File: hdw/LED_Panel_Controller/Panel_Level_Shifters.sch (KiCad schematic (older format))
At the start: 0 parts

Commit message: log's first
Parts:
- added C? (x2): 0.1uF, Capacitors_SMD:C_0603, symbol Custom_Library:C_Custom
- added R? (x2): 10K, Resistors_SMD:R_0603, symbol Custom_Library:R_Custom
- added RN? (x2): 10k, Resistors_SMD:R_Array_Convex_8x0602, symbol Device:R_Pack08
- added U? (x2): 74VHC541, Package_DFN_QFN:WQFN-20-1EP_2.5x4.5mm_P0.5mm_EP1x2.9mm, symbol Custom_Library:74VHC541
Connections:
- net labels added: +3.3V, +5V, GND, ~IO_Level_Shift_Enable
- wire segments 0 -> 94
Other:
- note added: "I/O Buffers"

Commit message: lots of schematic progress
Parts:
- added RN? (x2): 10k, Resistors_SMD:R_Array_Convex_8x0602, symbol Device:R_Pack08
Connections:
- net labels added: B0_POS3P3, B0_POS5, B1_POS3P3, B1_POS5, G0_POS3P3, G0_POS5, G1_POS3P3, G1_POS5, Panel_CLK_POS3P3, Panel_CLK_POS5, Panel_LAT_POS3P3, Panel_LAT_POS5, R0_POS3P3, R0_POS5, R1_POS3P3, R1_POS5, Row_A_POS3P3, Row_A_POS5, Row_B_POS3P3, Row_B_POS5, Row_C_POS3P3, Row_C_POS5, Row_D_POS3P3, Row_D_POS5, Row_E_POS3P3, Row_E_POS5, ~Panel_OE_POS3P3, ~Panel_OE_POS5
- wire segments 94 -> 172
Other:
- note removed: "I/O Buffers"
- moved on the sheet: C?, R?

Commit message: fixed level shifter sheet
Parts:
- removed R? (x2): 10K, Resistors_SMD:R_0603, symbol Custom_Library:R_Custom
- removed RN? (x4): 10k, Resistors_SMD:R_Array_Convex_8x0602, symbol Device:R_Pack08
- removed U? (x2): 74VHC541, Package_DFN_QFN:WQFN-20-1EP_2.5x4.5mm_P0.5mm_EP1x2.9mm, symbol Custom_Library:74VHC541
- added R? (x32): 10K, Resistors_SMD:R_0603, symbol Custom_Library:R_Custom
- added R? (x28): 10, Resistors_SMD:R_0402, symbol Custom_Library:R_Custom
- added U? (x2): 74HCT541, Housings_SSOP:SSOP-20_4.4x6.5mm_Pitch0.65mm, symbol 74xx:74HCT541
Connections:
- net labels added: ~Panel_Level_Shift_Enable
- net labels removed: ~IO_Level_Shift_Enable
- wire segments 172 -> 100
- no-connect marks 0 -> 2

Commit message: more schematic progress
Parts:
- removed U?: 74HCT541, Housings_SSOP:SSOP-20_4.4x6.5mm_Pitch0.65mm, symbol 74xx:74HCT541
- added U?: 74HCT541, Housings_SSOP:SSOP-20_4.4x6.5mm_Pitch0.65mm, symbol 74xx:74HCT541
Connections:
- net +5V: now also U?.20 (VCC)
- net GND: now also U?.10 (GND)
- net ~Panel_Level_Shift_Enable: now also U?.1 (G1), U?.19 (G2)
- net at R?.1, R?.1: now also U?.2 (A0)
- net at R?.1, R?.1: now also U?.3 (A1)
- net at R?.1, R?.1: now also U?.4 (A2)
- net at R?.1, R?.1: now also U?.5 (A3)
- net at R?.1, R?.1: now also U?.6 (A4)
- net at R?.1, R?.1: now also U?.7 (A5)
- net at R?.1, R?.1: now also U?.8 (A6)
- net at R?.1, R?.1: now also U?.9 (A7)
- net at R?.1, R?.1: now also U?.11 (Y7)
- net at R?.1, R?.1: now also U?.12 (Y6)
- net at R?.1, R?.1: now also U?.13 (Y5)
- net at R?.1, R?.1: now also U?.14 (Y4)
- net at R?.1, R?.1: now also U?.15 (Y3)
- net at R?.1, R?.1: now also U?.16 (Y2)
- net at R?.1, R?.1: now also U?.17 (Y1)
- net at R?.1, R?.1: now also U?.18 (Y0)
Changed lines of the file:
@@
-$EndComp
-$Comp
-L 74xx:74HCT541 U?
-U 1 1 60236D71
-P 5280 4750
-F 0 "U?" H 4980 5400 50  0000 C CNN
-F 1 "74HCT541" H 4980 4100 50  0000 C CNN
-F 2 "Housings_SSOP:SSOP-20_4.4x6.5mm_Pitch0.65mm" H 5280 4750 50  0001 C CNN
-F 3 "http://www.ti.com/lit/gpn/sn74HCT541" H 5280 4750 50  0001 C CNN
-F 4 "296-26499-1-ND" H 5280 4750 50  0001 C CNN "Digi-Key PN"
-	1    5280 4750
-	1    0    0    -1
 $EndComp
 $Comp
@@
 	0    -1   1    0
 $EndComp
+$Comp
+L 74xx:74HCT541 U?
+U 1 1 6019D5B0
+P 5280 4750
+F 0 "U?" H 4980 5400 50  0000 C CNN
+F 1 "74HCT541" H 4980 4100 50  0000 C CNN
+F 2 "Housings_SSOP:SSOP-20_4.4x6.5mm_Pitch0.65mm" H 5280 4750 50  0001 C CNN
+F 3 "http://www.ti.com/lit/gpn/sn74HCT541" H 5280 4750 50  0001 C CNN
+F 4 "296-26499-1-ND" H 5280 4750 50  0001 C CNN "Digi-Key PN"
+	1    5280 4750
+	1    0    0    -1
+$EndComp
 $EndSCHEMATC

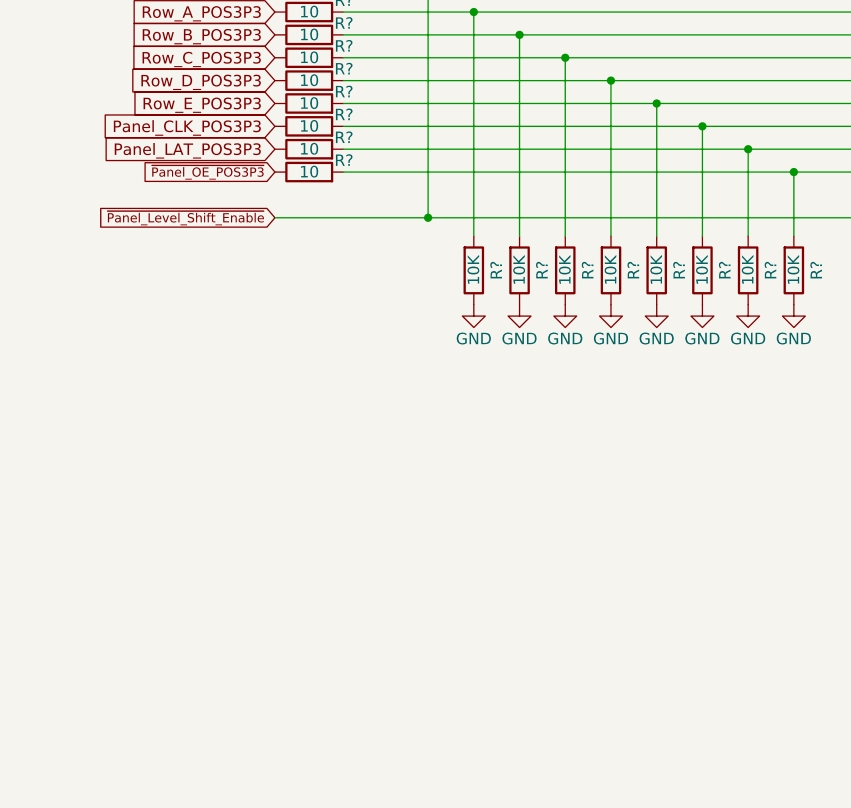
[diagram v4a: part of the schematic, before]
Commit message: Added panel dimming OR gate
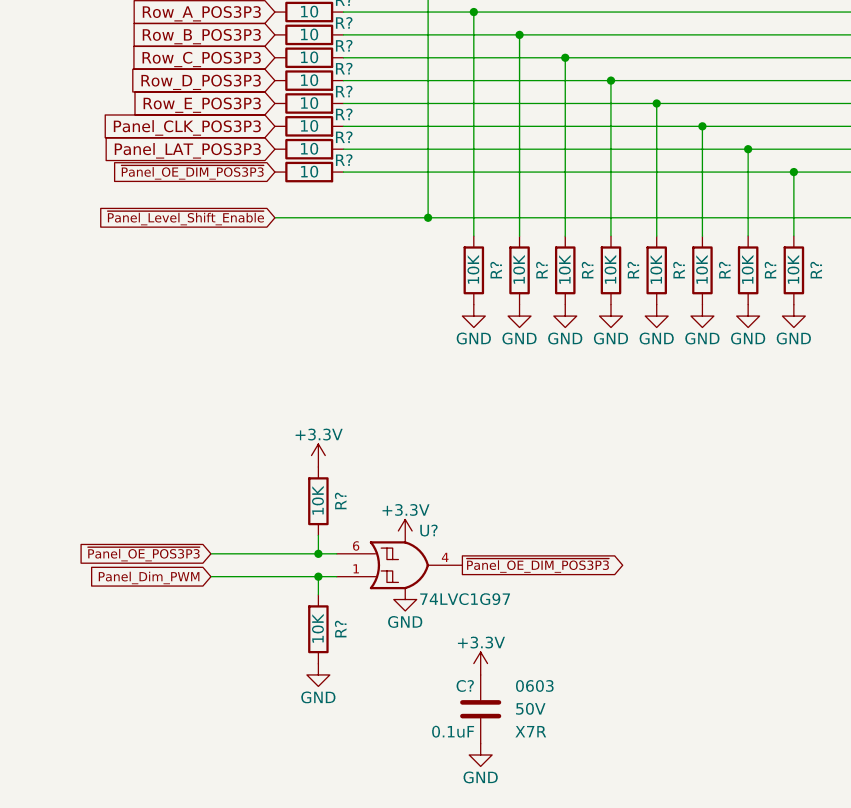
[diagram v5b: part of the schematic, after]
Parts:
- added C?: 0.1uF, Capacitors_SMD:C_0603, symbol Custom_Library:C_Custom
- added R? (x2): 10K, Resistors_SMD:R_0603, symbol Custom_Library:R_Custom
- added U?: 74LVC1G97, Package_TO_SOT_SMD:SOT-363_SC-70-6, symbol Custom_Library:74LVC1G97_Power_OR
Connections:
- net +3V3: now also C?.1, R?.1, U?.3 (VCC), U?.5 (VCC)
- net GND: now also C?.2, R?.2, U?.2 (GND)
- net ~Panel_OE_POS3P3: now also R?.2, U?.6; no longer R?.2
- new net Panel_Dim_PWM: R?.1, U?.1
- new net ~Panel_OE_DIM_POS3P3: R?.2, U?.4
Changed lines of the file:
@@
 Text GLabel 2060 4850 0    50   Input ~ 0
 Panel_LAT_POS3P3
-Text GLabel 2060 4950 0    40   Input ~ 0
-~Panel_OE_POS3P3
 Text GLabel 2060 4750 0    50   Input ~ 0
 Panel_CLK_POS3P3
@@
 	1    0    0    -1
 $EndComp
+Text GLabel 1780 6620 0    40   Input ~ 0
+~Panel_OE_POS3P3
+Text GLabel 1780 6720 0    40   Input ~ 0
+Panel_Dim_PWM
+$Comp
+L Custom_Library:74LVC1G97_Power_OR U?
+U 1 1 605B6BBC
+P 2630 6670
+F 0 "U?" H 2690 6820 50  0000 L CNN
+F 1 "74LVC1G97" H 2690 6520 50  0000 L CNN
+F 2 "Package_TO_SOT_SMD:SOT-363_SC-70-6" H 2680 6670 50  0001 C CNN
+F 3 "http://www.ti.com/lit/ds/symlink/sn74lvc1g97.pdf" H 2680 6670 50  0001 C CNN
+	1    2630 6670
+	1    0    0    -1
+$EndComp
+$Comp
+L power:GND #PWR?
+U 1 1 605B933E
+P 2630 6770
+F 0 "#PWR?" H 2630 6520 50  0001 C CNN
+F 1 "GND" H 2630 6620 50  0000 C CNN
+F 2 "" H 2630 6770 50  0001 C CNN
+F 3 "" H 2630 6770 50  0001 C CNN
+	1    2630 6770
+	1    0    0    -1
+$EndComp
+$Comp
+L power:+3.3V #PWR?
+U 1 1 605B9C84
+P 2630 6570
+F 0 "#PWR?" H 2630 6420 50  0001 C CNN
+F 1 "+3.3V" H 2630 6710 50  0000 C CNN
+F 2 "" H 2630 6570 50  0001 C CNN
+F 3 "" H 2630 6570 50  0001 C CNN
+	1    2630 6570
+	1    0    0    -1
+$EndComp
+Text GLabel 2880 6670 2    40   Output ~ 0
+~Panel_OE_DIM_POS3P3
+Text GLabel 2060 4950 0    40   Input ~ 0
+~Panel_OE_DIM_POS3P3
+$Comp
+L Custom_Library:R_Custom R?
+U 1 1 605BD1A0
+P 2250 6950
+AR Path="/5BAAE2B6/605BD1A0" Ref="R?"  Part="1"
+AR Path="/5BB6CF6D/605BD1A0" Ref="R?"  Part="1"
+AR Path="/5BBE424C/605BD1A0" Ref="R?"  Part="1"
+AR Path="/5CB8A16A/605BD1A0" Ref="R?"  Part="1"
+AR Path="/5F583BF6/605BD1A0" Ref="R?"  Part="1"
+F 0 "R?" V 2150 6950 50  0000 C CNN
+F 1 "10K" V 2250 6950 50  0000 C CNN
+F 2 "Resistors_SMD:R_0603" H 2250 6950 50  0001 C CNN
+F 3 "" H 2250 6950 50  0001 C CNN
+F 4 "0603" H 2320 7040 50  0001 L CNN "display_footprint"
+F 5 "1%" H 2320 6950 50  0001 L CNN "Tolerance"
+F 6 "1/10W" H 2320 6870 50  0001 L CNN "Wattage"
+F 7 "RHM10KADCT-ND" H 2550 7350 60  0001 C CNN "Digi-Key PN"
+	1    2250 6950
+	-1   0    0    -1
+$EndComp
+$Comp
+L power:GND #PWR?
+U 1 1 605BD6BC
+P 2250 7100
+F 0 "#PWR?" H 2250 6850 50  0001 C CNN
+F 1 "GND" H 2250 6950 50  0000 C CNN
+F 2 "" H 2250 7100 50  0001 C CNN
+F 3 "" H 2250 7100 50  0001 C CNN
+	1    2250 7100
+	1    0    0    -1
+$EndComp
+$Comp
+L Custom_Library:R_Custom R?
+U 1 1 605BD8E0
+P 2250 6390
+AR Path="/5BAAE2B6/605BD8E0" Ref="R?"  Part="1"
+AR Path="/5BB6CF6D/605BD8E0" Ref="R?"  Part="1"
+AR Path="/5BBE424C/605BD8E0" Ref="R?"  Part="1"
+AR Path="/5CB8A16A/605BD8E0" Ref="R?"  Part="1"
+AR Path="/5F583BF6/605BD8E0" Ref="R?"  Part="1"
+F 0 "R?" V 2150 6390 50  0000 C CNN
+F 1 "10K" V 2250 6390 50  0000 C CNN
+F 2 "Resistors_SMD:R_0603" H 2250 6390 50  0001 C CNN
+F 3 "" H 2250 6390 50  0001 C CNN
+F 4 "0603" H 2320 6480 50  0001 L CNN "display_footprint"
+F 5 "1%" H 2320 6390 50  0001 L CNN "Tolerance"
+F 6 "1/10W" H 2320 6310 50  0001 L CNN "Wattage"
+F 7 "RHM10KADCT-ND" H 2550 6790 60  0001 C CNN "Digi-Key PN"
+	1    2250 6390
+	-1   0    0    -1
+$EndComp
+Wire Wire Line
+	2330 6620 2250 6620
+Wire Wire Line
+	2250 6620 2250 6540
+Wire Wire Line
+	2330 6720 2250 6720
+Wire Wire Line
+	2250 6720 2250 6800
+$Comp
+L Custom_Library:C_Custom C?
+U 1 1 605C5437
+P 2960 7300
+AR Path="/5BAAE1F3/605C5437" Ref="C?"  Part="1"
+AR Path="/5BAAE1CB/605C5437" Ref="C?"  Part="1"
+AR Path="/5BE48F98/605C5437" Ref="C?"  Part="1"
+AR Path="/5CAD2D97/605C5437" Ref="C?"  Part="1"
+AR Path="/5CB7A8BC/605C5437" Ref="C?"  Part="1"
+AR Path="/5CB7A8C3/605C5437" Ref="C?"  Part="1"
+AR Path="/5CB8A16A/605C5437" Ref="C?"  Part="1"
+AR Path="/5F583BF6/605C5437" Ref="C?"  Part="1"
+F 0 "C?" H 2985 7400 50  0000 L CNN
+F 1 "0.1uF" H 2985 7200 50  0000 L CNN
+F 2 "Capacitors_SMD:C_0603" H 2998 7150 50  0001 C CNN
+F 3 "" H 2985 7400 50  0001 C CNN
+F 4 "311-1344-1-ND" H 3385 7800 60  0001 C CNN "Digi-Key PN"
+F 5 "0603" H 2810 7400 50  0000 R CNN "display_footprint"
+F 6 "50V" H 2810 7300 50  0000 R CNN "Voltage"
+F 7 "X7R" H 2810 7200 50  0000 R CNN "Dielectric"
+	1    2960 7300
+	-1   0    0    -1
+$EndComp
+$Comp
+L power:GND #PWR?
+U 1 1 605C543D
+P 2960 7450
+AR Path="/5CB7A8BC/605C543D" Ref="#PWR?"  Part="1"
+AR Path="/5CB7A8C3/605C543D" Ref="#PWR?"  Part="1"
+AR Path="/5CB8A16A/605C543D" Ref="#PWR?"  Part="1"
+AR Path="/5F583BF6/605C543D" Ref="#PWR?"  Part="1"
+F 0 "#PWR?" H 2960 7200 50  0001 C CNN
+F 1 "GND" H 2960 7300 50  0000 C CNN
+F 2 "" H 2960 7450 50  0001 C CNN
+F 3 "" H 2960 7450 50  0001 C CNN
+	1    2960 7450
+	1    0    0    -1
+$EndComp
+$Comp
+L power:+3.3V #PWR?
+U 1 1 605C8091
+P 2960 7150
+F 0 "#PWR?" H 2960 7000 50  0001 C CNN
+F 1 "+3.3V" H 2960 7290 50  0000 C CNN
+F 2 "" H 2960 7150 50  0001 C CNN
+F 3 "" H 2960 7150 50  0001 C CNN
+	1    2960 7150
+	1    0    0    -1
+$EndComp
+Wire Wire Line
+	1780 6720 2250 6720
+Connection ~ 2250 6720
+Wire Wire Line
+	1780 6620 2250 6620
+Connection ~ 2250 6620
+$Comp
+L power:+3.3V #PWR?
+U 1 1 605CEF05
+P 2250 6240
+F 0 "#PWR?" H 2250 6090 50  0001 C CNN
+F 1 "+3.3V" H 2250 6380 50  0000 C CNN
+F 2 "" H 2250 6240 50  0001 C CNN
+F 3 "" H 2250 6240 50  0001 C CNN
+	1    2250 6240
+	1    0    0    -1
+$EndComp

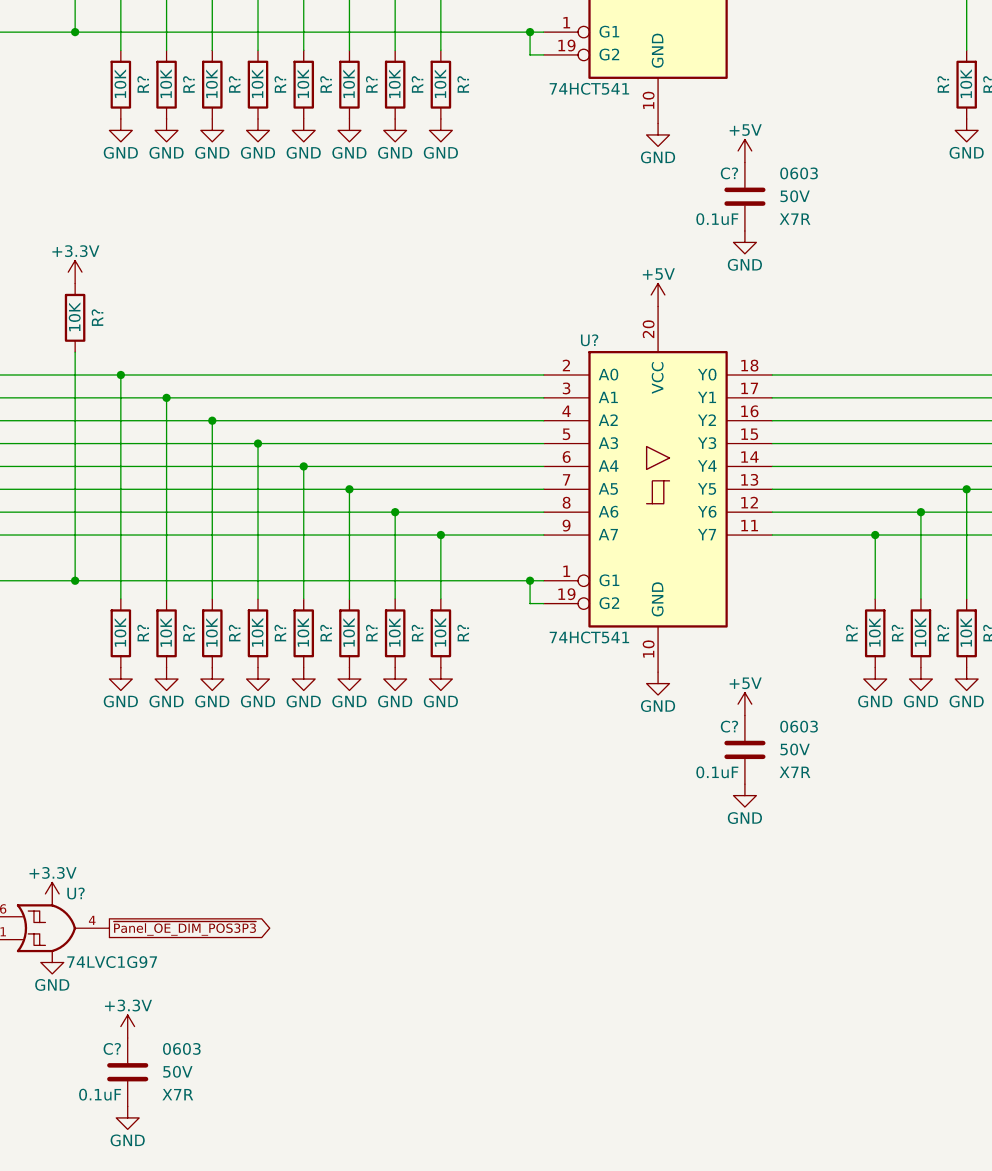
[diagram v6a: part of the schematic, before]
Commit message: added digikey pns, footprints, bom scrubbed
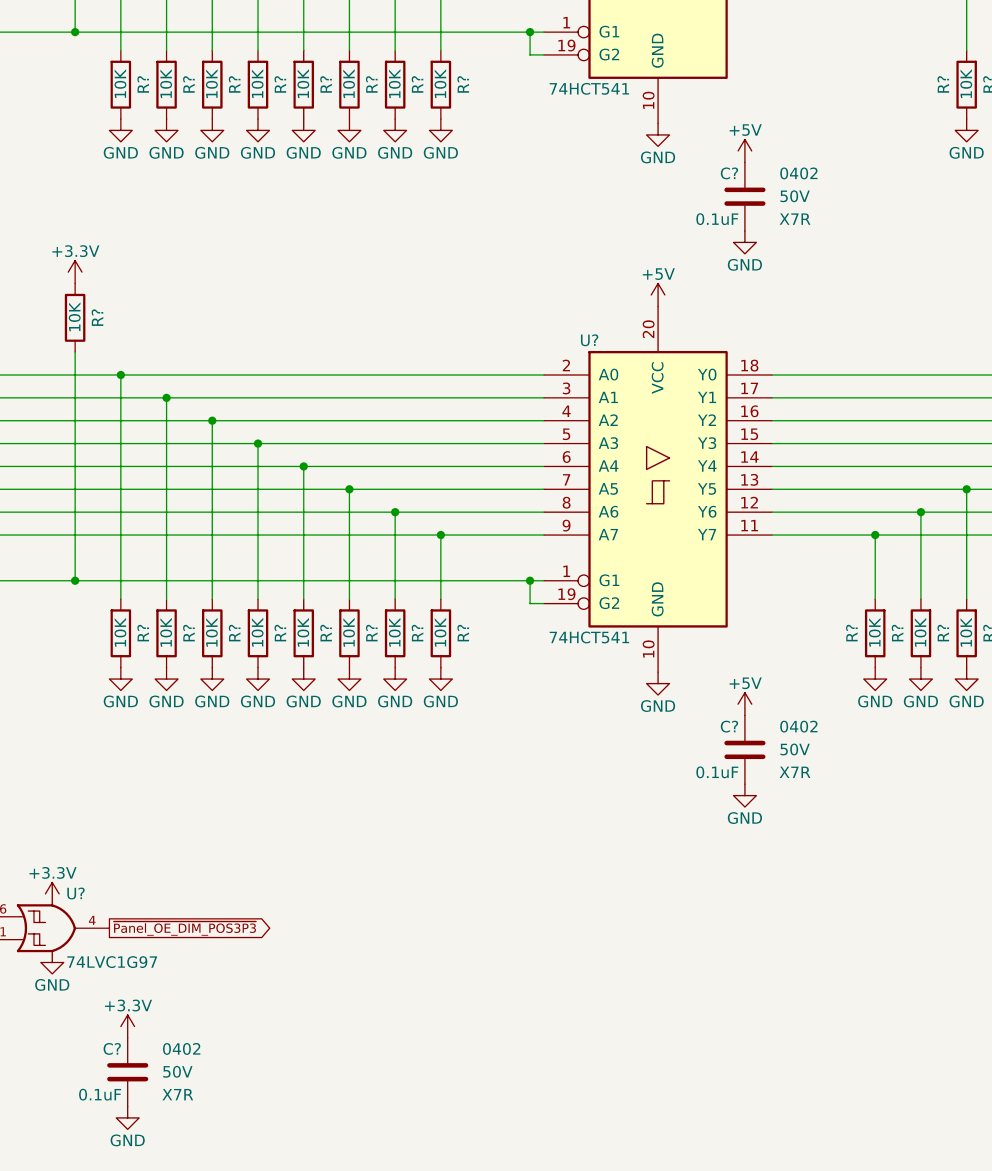
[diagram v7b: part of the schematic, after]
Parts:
- C? (x3): footprint Capacitors_SMD:C_0603 -> Capacitors_SMD:C_0402; Digi-Key PN 311-1344-1-ND -> 490-10701-1-ND; display_footprint 0603 -> 0402
- R? (x34): footprint Resistors_SMD:R_0603 -> Resistors_SMD:R_0402; Digi-Key PN RHM10KADCT-ND -> RMCF0402FT10K0CT-ND; Wattage 1/10W -> 1/16W; display_footprint 0603 -> 0402
- R? (x28): Digi-Key PN (none) -> RMCF0402FT10R0CT-ND
- U?: Digi-Key PN (none) -> 1727-1772-1-ND
